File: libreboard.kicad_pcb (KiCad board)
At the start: 6 copper layers, 125 x 125 mm, 218 parts, among them J1 USB-C, J10 USB-C, J100 Screw Terminal, J101 Screw Terminal, J11 USB_C_Receptacle_USB2.0, J14 JST_BM04B-SRSS-TB, J15 USB_C_Receptacle, J16 JST_BM04B-SRSS-TB, J17 USB-C, J19 Conn_1x03_Male, J2 Conn_2x07_Male, J22 Conn_HDMI, J3 Conn_1x03_Male, J4 Bus_M.2_Socket_M, J5 Conn_1x22_Female, J51 12V Fan 1, J52 12V Fan 2, J53 12V Fan 3, J54 12V Fan 4, J6 USB-C, J7 Micro_SD_Card_Det, J8 Conn_2x20_Male, Q1 2N7002, Q2 2N7002, SW1 Right angle Tact button, SW2 Right angle Tact button, U1 TPD4EUSB30, U10 EMC2305-x-AP, U11 TUSB4041I, U12 RT9742SNGV, U13 TLV75712PDBVR, U14 TPS552892RYQR, U15 AP22653W6, U16 SN74AHCT1G125DRLR, U17 TCA9538DBR, U18 RT9742GGJ5, U19 TPS3808G01DBVR, U2 TPD4EUSB30, U20 LP38693MP-3.3, U21 HD3SS3220RNHR, U3 MagJack-A70-112-331N126, U4 TPS552892RYQR, U5 74LVC1G07SE-7, U6 AP22653W6, U7 ASEK-32.768KHZ-L-R-T, U8 AP3441SHE-7B, U9 SK6812, Y1 ECS-2520MV-240-CN-TR

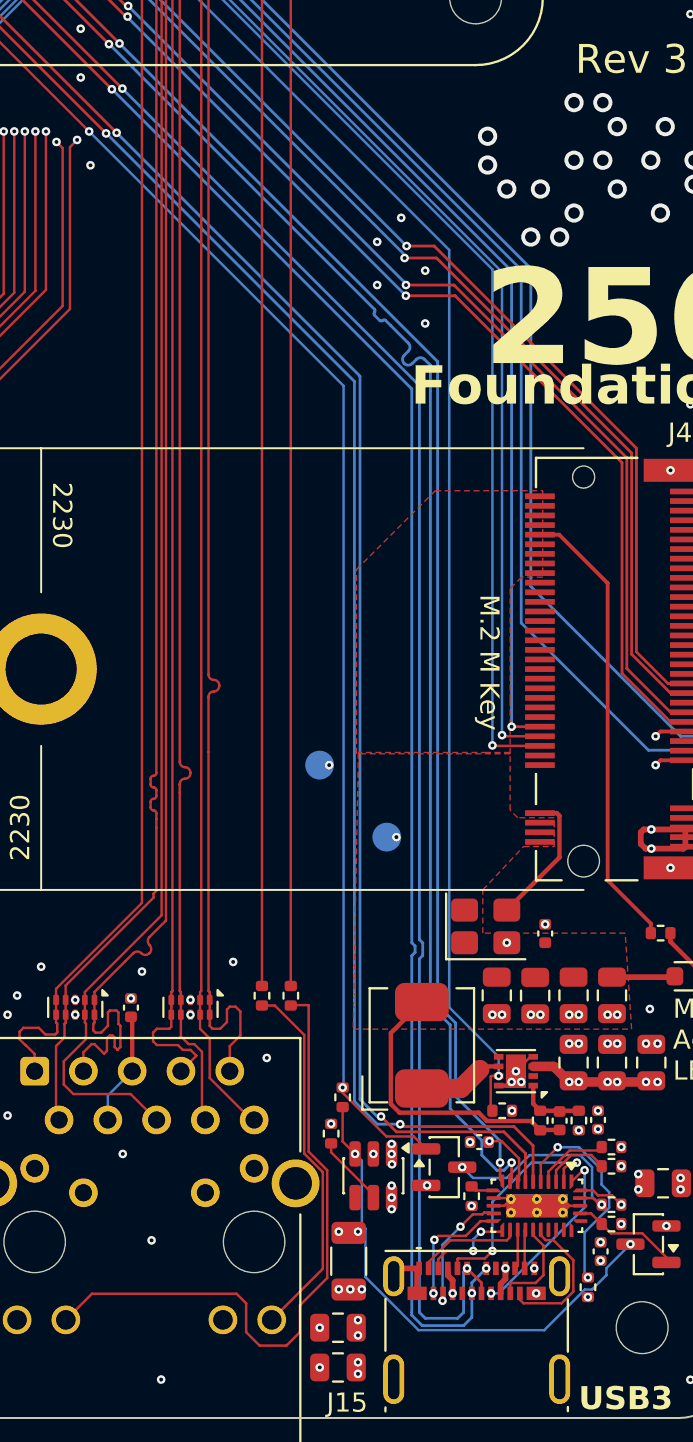
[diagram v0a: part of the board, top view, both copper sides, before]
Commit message: PCB: J15 SuperSpeed pairs at 90R, intra-pair skew matched
Michael's rework after 3d6803a and ded29a1:
- J15_TX1/TX2/RX1/RX2 re-routed with the 90R pair geometry
  (0.147 mm); the RX2 fan-out no longer runs 0.053 mm apart (narrowest
  P-N gap now 0.24 mm).
- Intra-pair skew, with via heights counted (use_height_for_length_calcs):
  J15_TX1 0.03 mm, J15_TX2 0.01, J15_RX1 0.02, J15_RX2 0.04,
  USB3-0-TX 0.11, USB3-0-RX 0.13 (was 3.55 mm).
  J15_TX1_N still changes to B.Cu and back on its own; it is matched
  to P by length, vias included.

DRC with schematic parity, with and without zone refill, matches
ded29a1: 0 unconnected, no new violations, only the four old J11
parity items.

Co-Authored-By: Claude Opus 5.5 <noreply@anthropic.com>
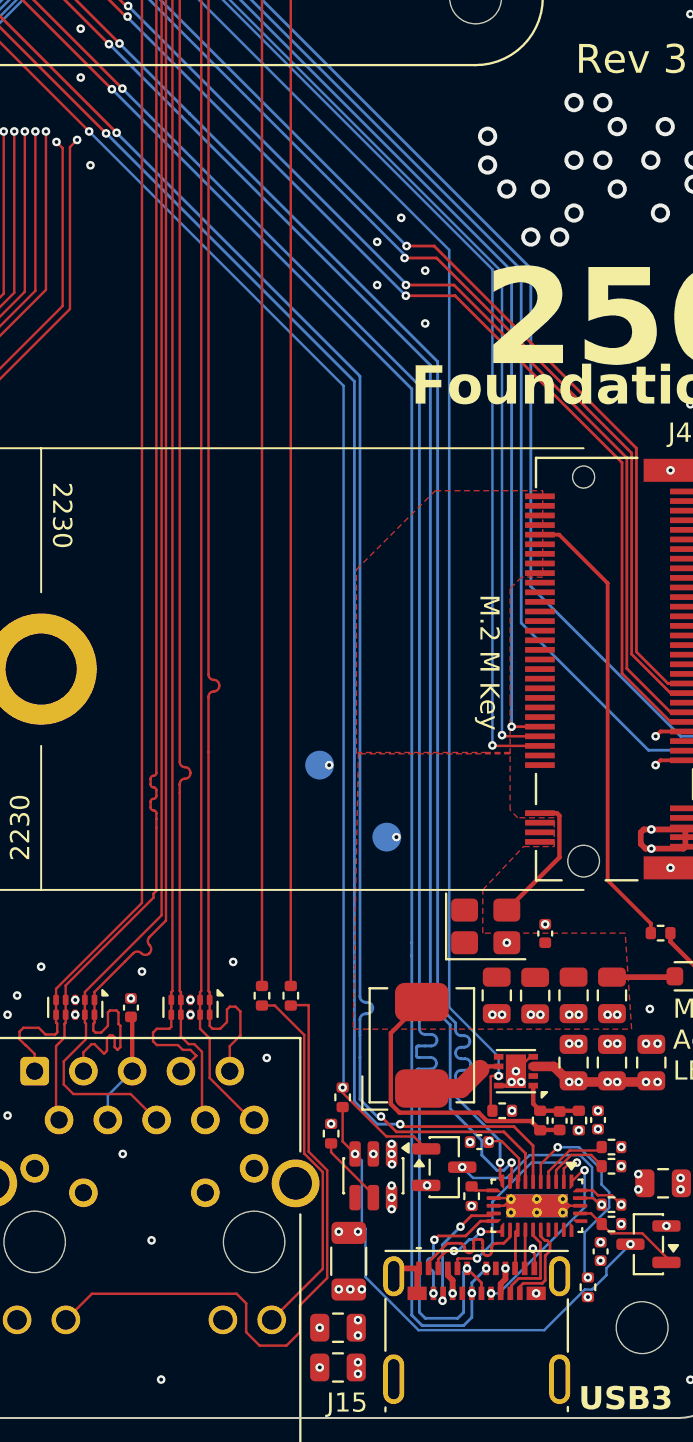
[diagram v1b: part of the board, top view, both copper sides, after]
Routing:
- net /CM5_HighSpeed/USB3-0-D_P: track 119.3 -> 123.6 mm
- net /CM5_HighSpeed/J15_TX2_P: track 7.60 -> 4.82 mm
- net /CM5_HighSpeed/USB3-0-RX_N: track 105.5 -> 107.5 mm
- net /CM5_HighSpeed/J15_TX1_P: track 5.49 -> 7.43 mm
- net /CM5_HighSpeed/USB3-0-RX_P: track 109.1 -> 107.6 mm
- net GND: track 257.2 -> 258.4 mm
- net /CM5_HighSpeed/USB3-0-TX_N: track 114.1 -> 114.8 mm
